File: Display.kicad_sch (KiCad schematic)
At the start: 6 parts

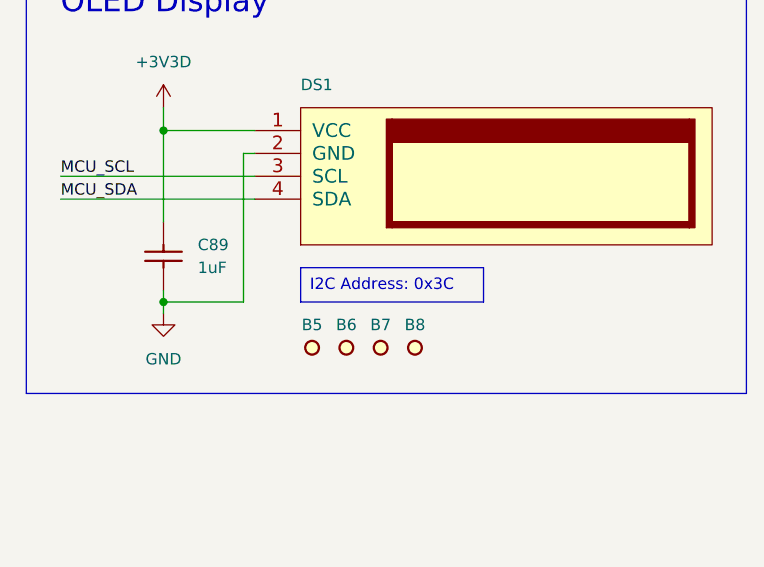
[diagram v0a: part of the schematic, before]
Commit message: Rename Power Supply sheet, remove iCE programming option
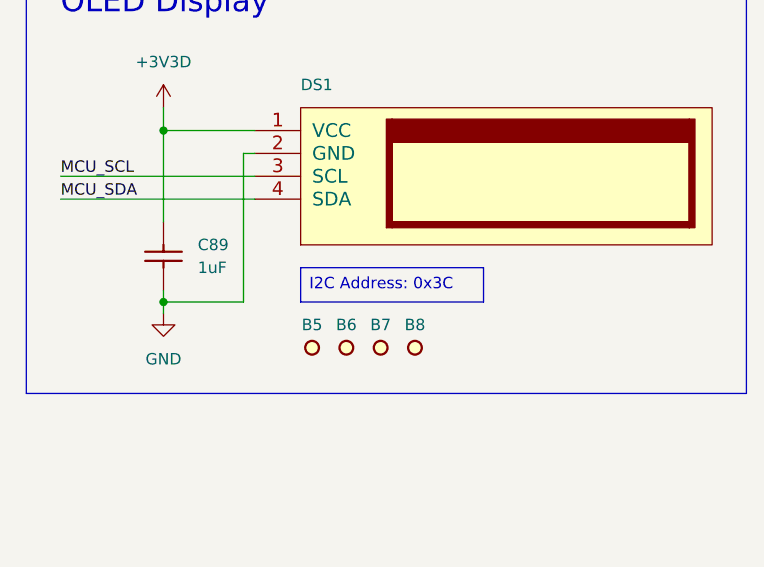
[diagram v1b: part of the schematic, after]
